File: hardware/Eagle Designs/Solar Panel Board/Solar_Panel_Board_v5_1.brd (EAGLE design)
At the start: 82.4 x 96.7 mm, 44 parts, among them J1 MOLEX_503763-0291MOLEX_503763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, J2 MOLEX_503763-0491MOLEX_503763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, J3 MOLEX_503763-0291MOLEX_503763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, U1 TMP36GSZ, U2 INA219BIDR

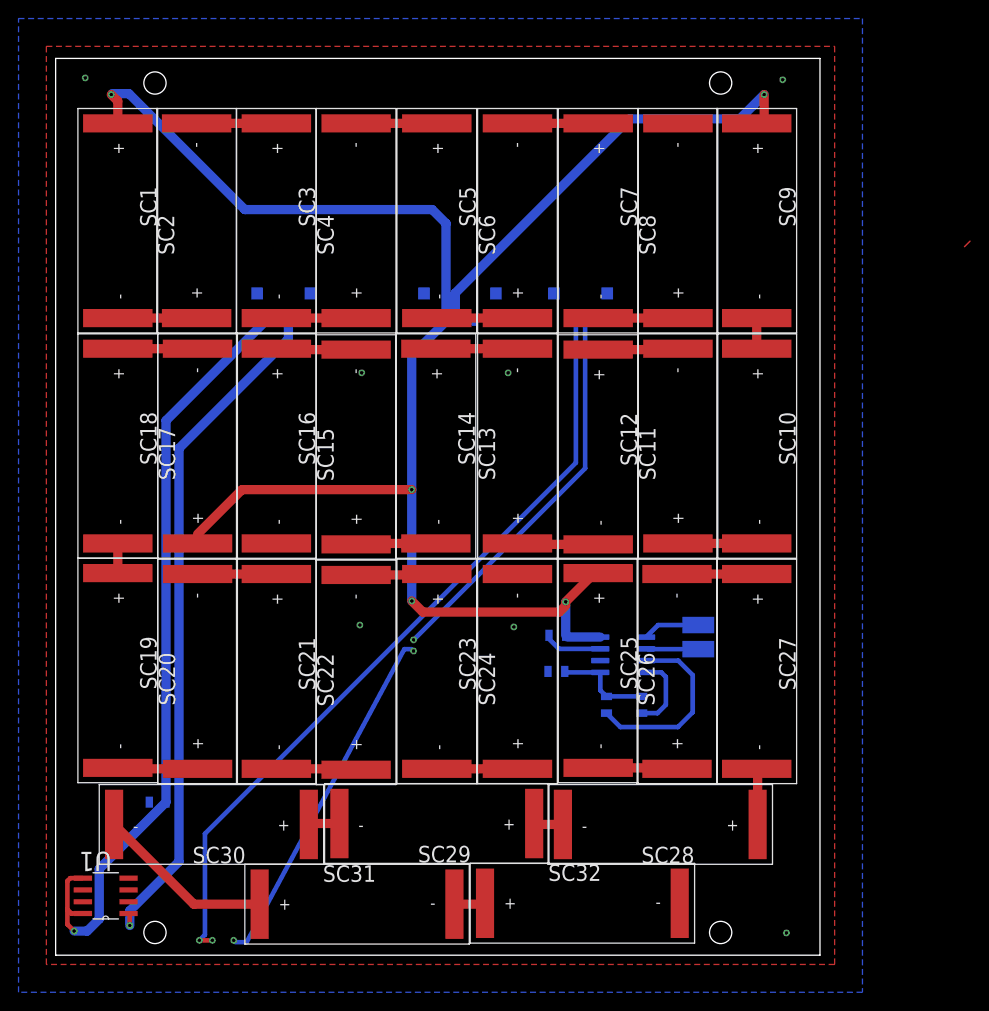
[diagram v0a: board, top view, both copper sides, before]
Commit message: made improvements to the solar panel board and included cam outputs
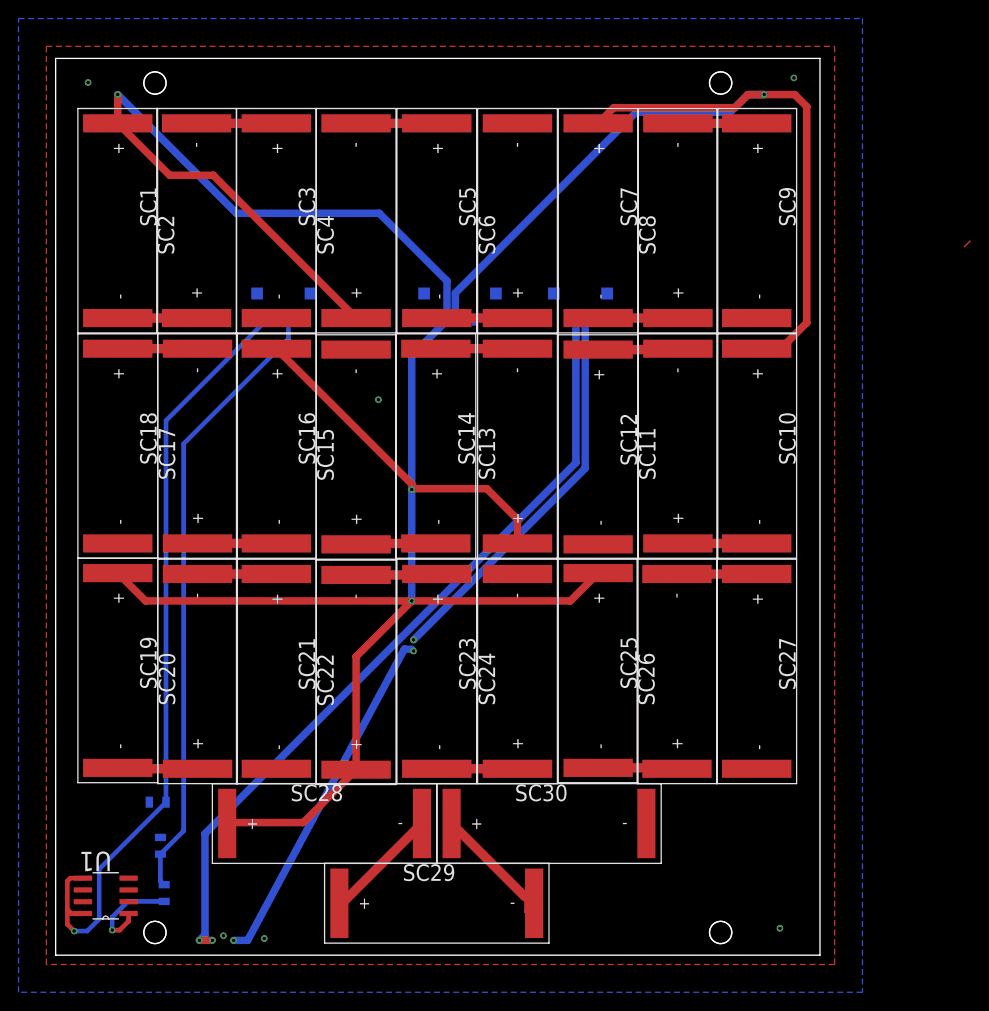
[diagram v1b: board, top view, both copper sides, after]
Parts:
- removed C2: 0.1uF, HSFL_Main_Library:0805
- removed R3: 2m, HSFL_Main_Library:0805
- removed SC31, SC32: KXOB25-05X3F, untitled:KXOB25-05X3F
- removed U$1, U$2: TEST_POINT, HSFL_Main_Library:TEST_POINT
- removed U2: INA219BIDR, INA219BIDR:SOIC127P599X175-8N
- R1: value 3.3k -> 27k
- R2: value 3.3k -> 10k
- moved R2 54.1 mm to (11.3, 11.8)
- moved R1 51.8 mm to (11.7, 6.70)
- moved SC30 36.4 mm to (53.2, 14.2), turned to 0 degrees
- moved SC28 36.2 mm to (29.0, 14.2), turned to 0 degrees
- moved SC29 8.60 mm to (41.1, 5.60), turned to 0 degrees
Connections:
- removed net N$16: SC21.-, SC22.+
- removed net N$17: SC18.-, SC19.+
- removed net N$20: SC31.-, SC32.+
- removed net N$25: SC27.-, SC28.+
- removed net N$31: U$1.1, U2.2
- removed net N$32: U$2.1, U2.1
- removed net N$33: R2.2, U2.4
- removed net N$36: R1.2, U2.3
- removed net VS: C2.1, R1.1, R2.1, U2.5
- net GND: now also R2.1, SC12.-, SC15.-, SC18.-, SC21.-, SC27.-, SC3.-, SC30.-, SC6.-, SC9.-; no longer C2.2, R3.2, SC16.-, SC32.-, SC8.-, U2.6, U2.7
- net N$12: now also R1.2, U1.1; no longer SC10.+, SC9.-
- net N$21: no longer SC30.-, SC31.+
- net N$3: no longer SC6.-, SC7.+
- net N$7: now also SC8.-, SC9.+; no longer SC3.-, SC4.+
- net N$8: now also SC16.-, SC17.+; no longer SC15.-, SC16.+
- net N$9: no longer SC12.-, SC13.+
- net VCC: now also SC10.+, SC13.+, SC16.+, SC19.+, SC22.+, SC28.+, SC4.+, SC7.+; no longer R3.1, SC17.+, SC9.+, U2.8
- net VOUT: now also R1.1, R2.2; no longer U1.1
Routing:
- net VCC: track 193.7 -> 345.6 mm, vias 5 -> 4
- net N$36: track 20.3 -> 0.00 mm
- net N$22: track 3.34 -> 14.3 mm
- net VS: track 10.5 -> 0.00 mm
- net N$21: track 22.4 -> 12.5 mm
- net N$9: track 17.4 -> 8.64 mm
- net N$3: track 18.8 -> 10.1 mm
- net N$16: track 8.64 -> 0.00 mm
- net N$33: track 8.31 -> 0.00 mm
- net N$12: track 3.30 -> 10.7 mm, vias 0 -> 1
- net VOUT: track 73.6 -> 66.6 mm, vias 1 -> 0
- net N$32: track 6.17 -> 0.00 mm
- net N$25: track 6.04 -> 0.00 mm
- net N$31: track 5.64 -> 0.00 mm
- net N$20: track 3.34 -> 0.00 mm
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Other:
- outline, holes or cut-outs redrawn
